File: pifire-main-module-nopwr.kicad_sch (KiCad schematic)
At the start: 36 parts, among them J1 GPIO, J10 Relay_Fan_JST, J11 AUX GPIO_PWR, J12 5V_ONOFF, J13 1WIRE_TEST, J14 PWR_SW, J15 BUTTONS_ENCODER, J2 SPI_DISPLAY, J4 12V_IN, J5 5V_IN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

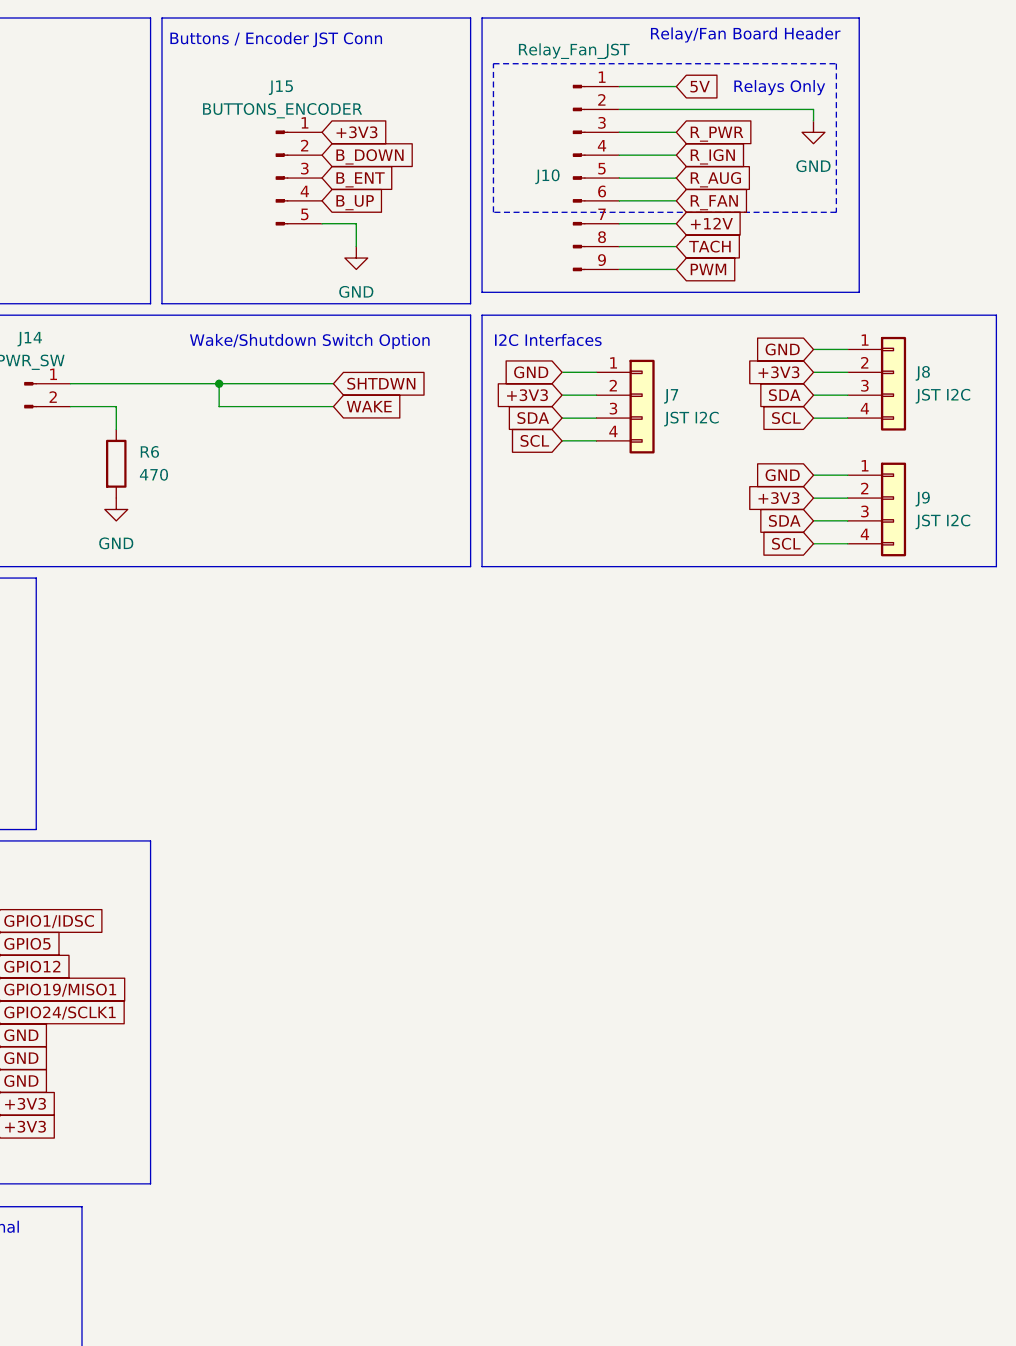
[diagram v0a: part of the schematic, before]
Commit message: Updated to v4.0.2
Split PWM pins out of the Relay/Fan header to create two headers.  This makes the board design more modular going forward and makes it easier to source the smaller 6 pin JST header.
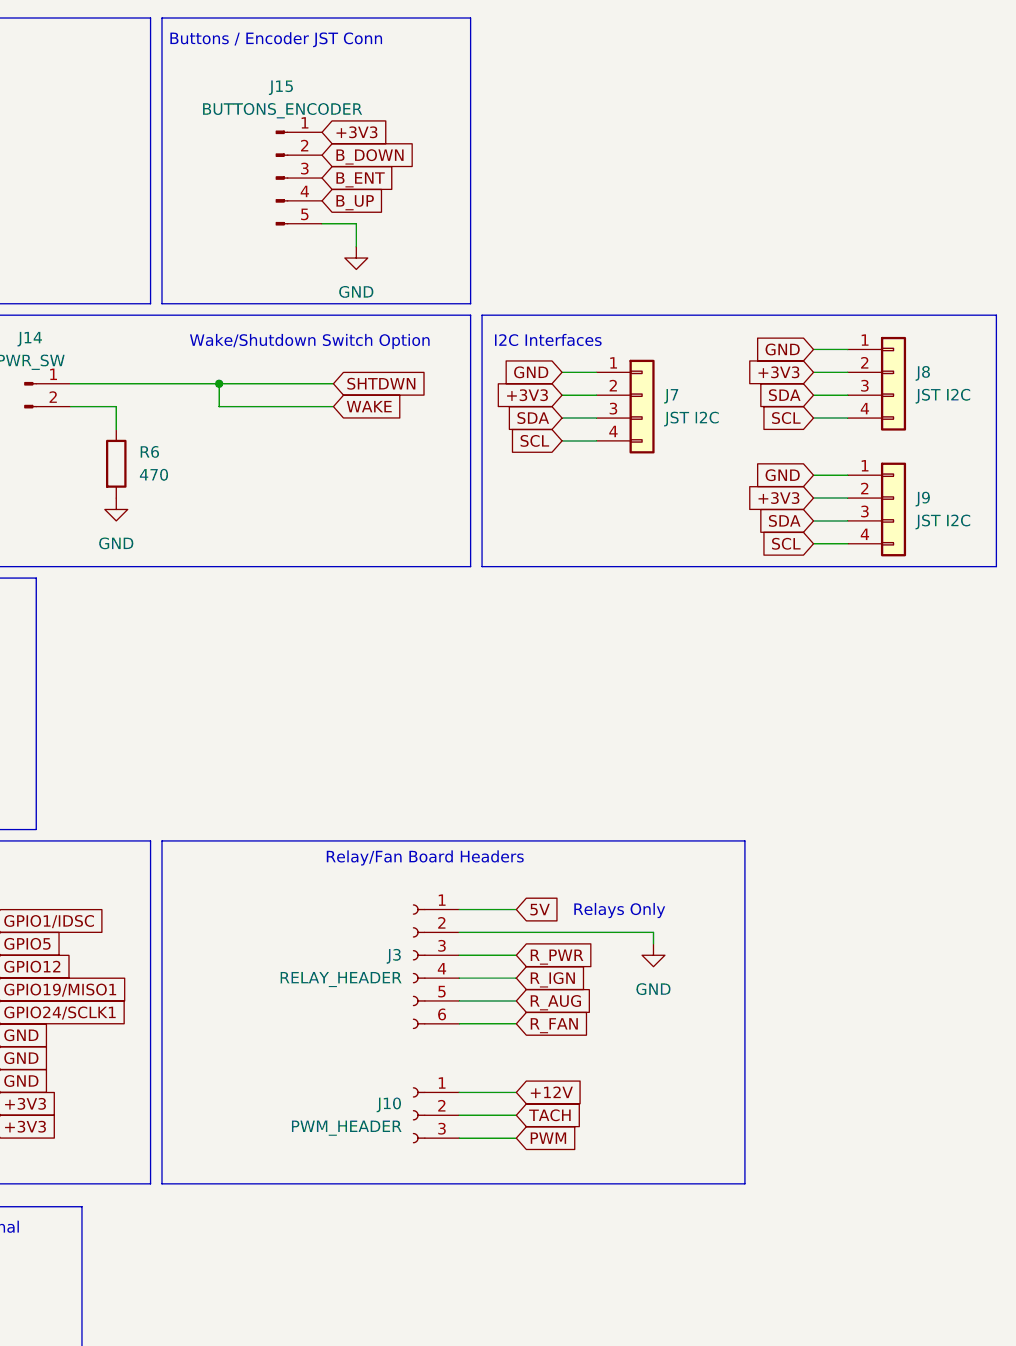
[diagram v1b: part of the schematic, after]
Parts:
- removed J10: Relay_Fan_JST, Connector_JST:JST_XH_B9B-XH-A_1x09_P2.50mm_Vertical, symbol Connector:Conn_01x09_Pin
- added J10: PWM_HEADER, Connector_JST:JST_XH_B3B-XH-A_1x03_P2.50mm_Vertical, symbol Connector:Conn_01x03_Socket
- added J3: RELAY_HEADER, Connector_JST:JST_XH_B6B-XH-A_1x06_P2.50mm_Vertical, symbol Connector:Conn_01x06_Socket
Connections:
- net +12V: now also J10.1 (Pin_1)
- net 5V: now also J3.1 (Pin_1)
- net GND: now also J3.2 (Pin_2)
- net GPIO27: now also J10.2 (Pin_2)
- net PWM: now also J10.3 (Pin_3)
- net R_AUG: now also J3.5 (Pin_5)
- net R_FAN: now also J3.6 (Pin_6)
- net R_IGN: now also J3.4 (Pin_4)
- net R_PWR: now also J3.3 (Pin_3)
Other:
- note added: "Relay/Fan Board Headers"
- note removed: "Relay/Fan Board Header"
